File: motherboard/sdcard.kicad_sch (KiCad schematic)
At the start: 9 parts, among them J14 Micro_SD_Card_Det1, U18 TPD4E02B04, U19 TPD4E02B04

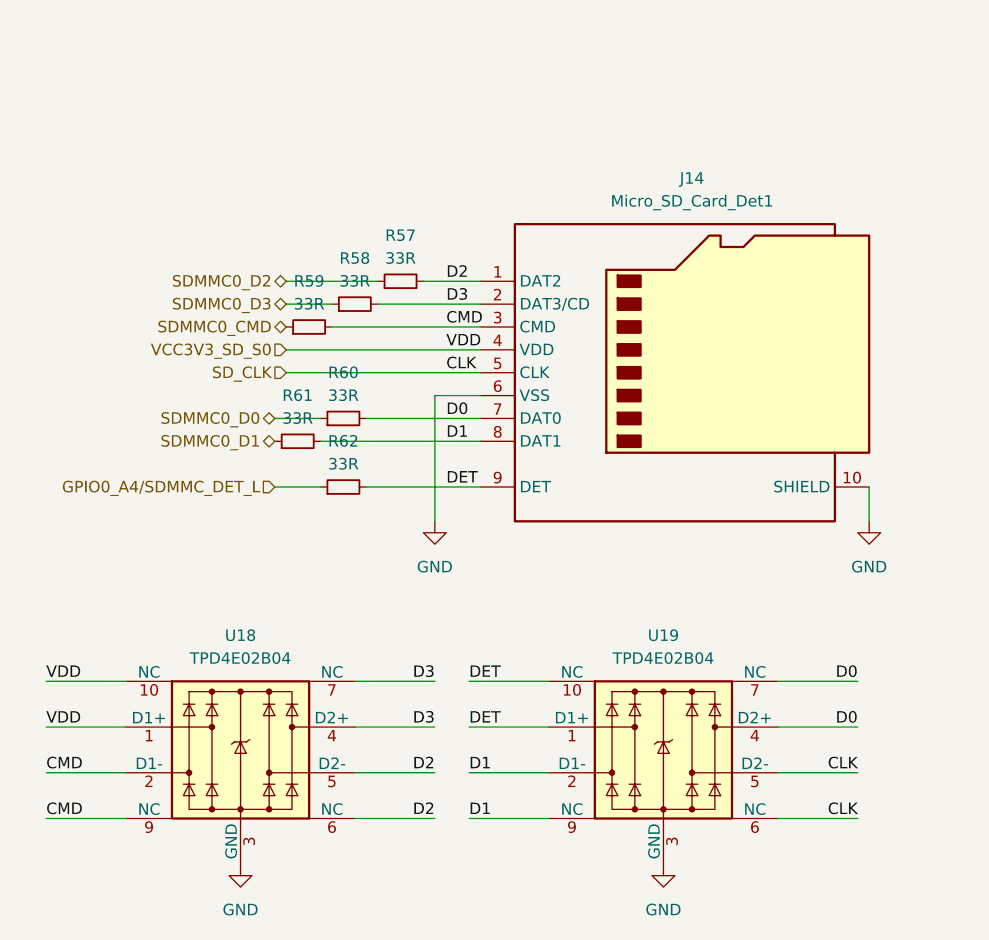
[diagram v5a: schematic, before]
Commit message: starting motherboard v0.2
lessons from display eval v1
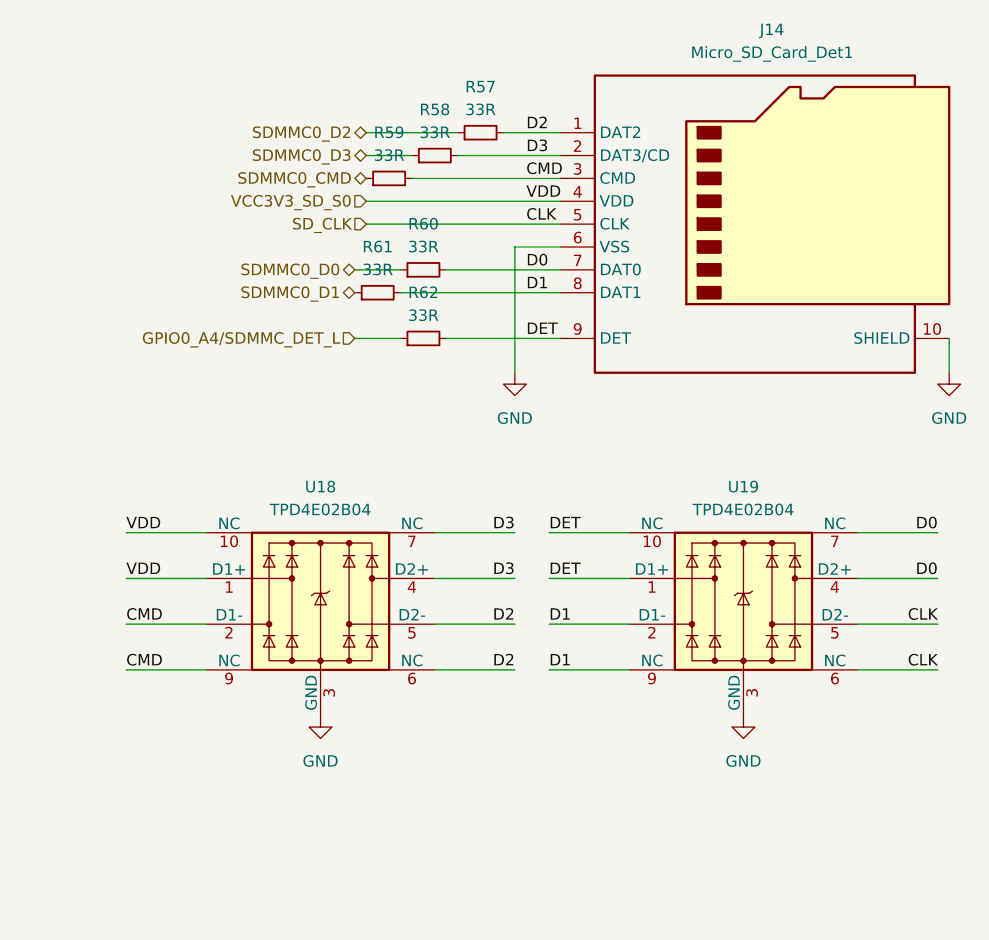
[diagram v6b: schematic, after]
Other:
- moved on the sheet: J14, R57, R58, R59, R60, R61, R62, U18, U19
